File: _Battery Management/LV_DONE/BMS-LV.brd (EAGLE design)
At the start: 94.8 x 46.2 mm, 119 parts, among them J1 M1x5, J2 M1x4, J3 M1x4, J4 M1x4, J5 M1x2, J6 MX150L, J8 M1x5, J9 M80022232081-2, K1 ADJ14024, Q2 40V 0.2A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

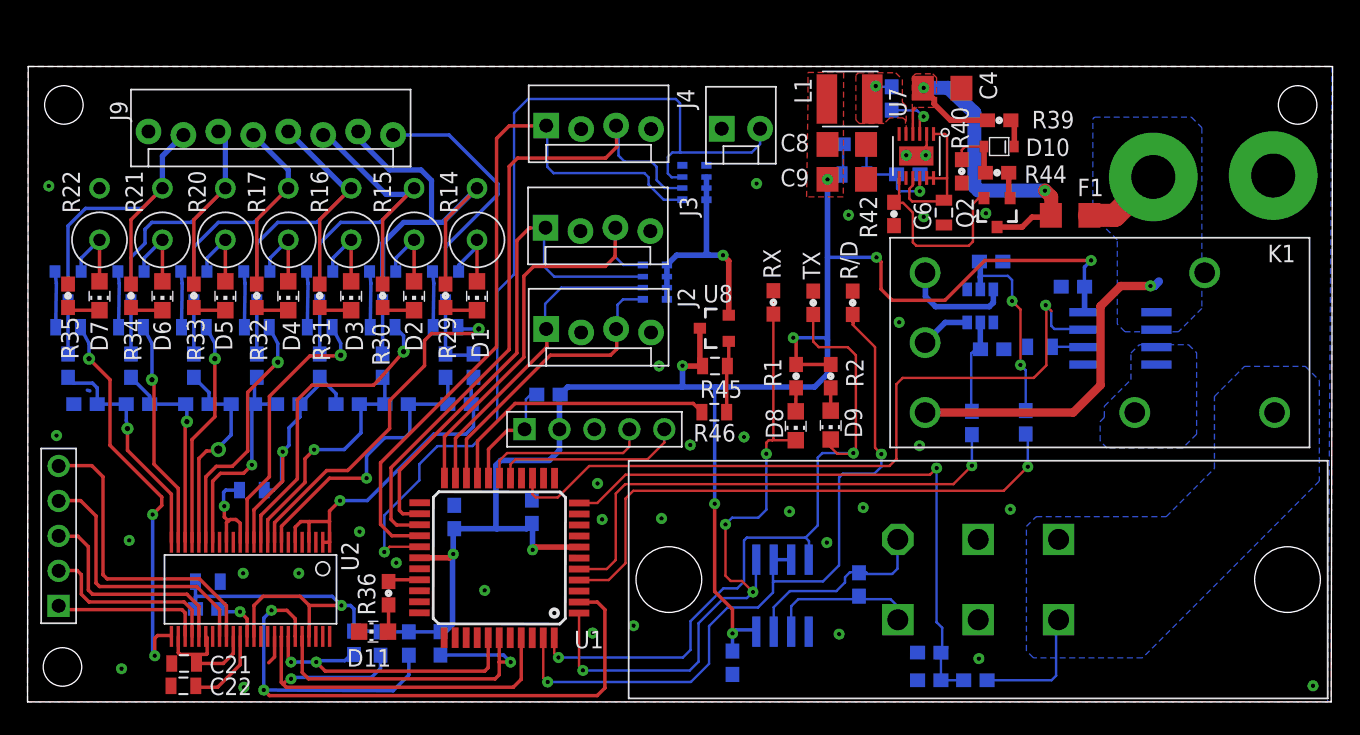
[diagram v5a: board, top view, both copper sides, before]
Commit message: 
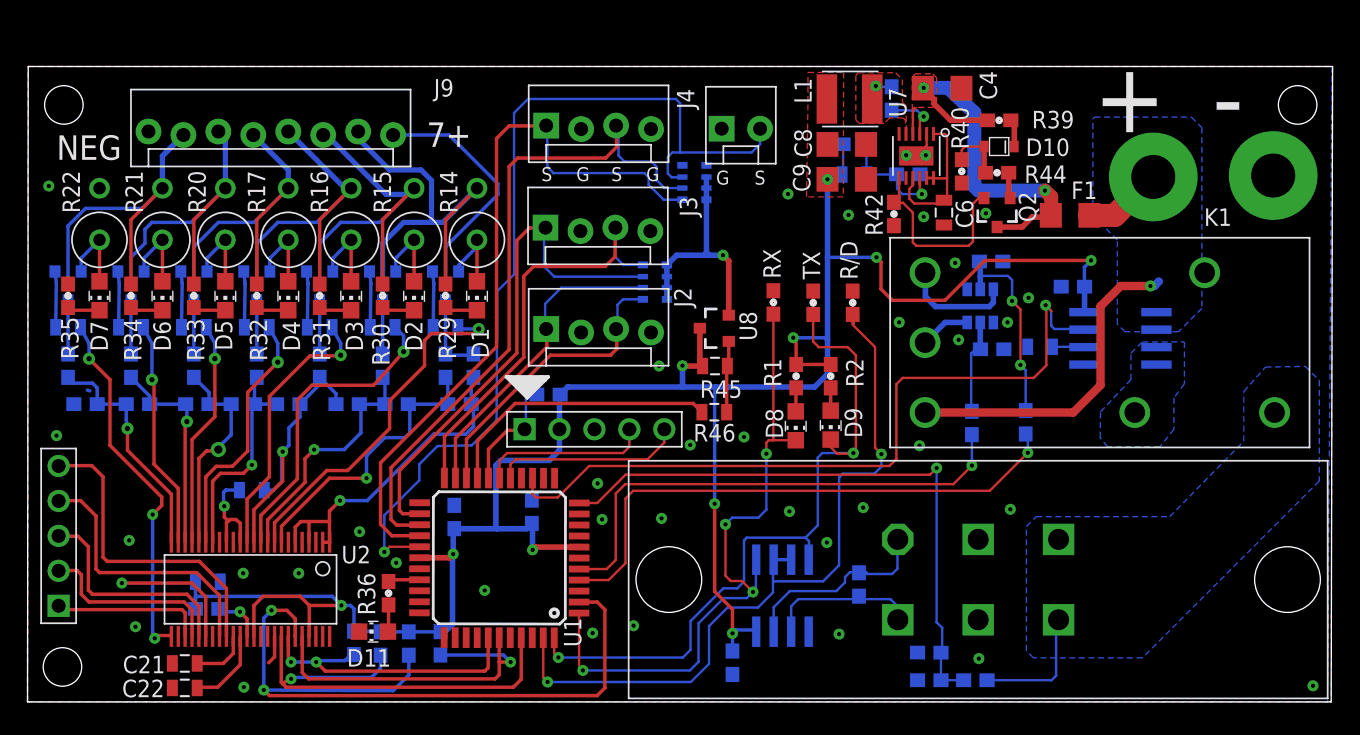
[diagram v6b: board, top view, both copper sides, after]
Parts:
- moved C22 0.18 mm to (11.4, 1.02)
- moved C21 0.05 mm to (11.4, 2.79)
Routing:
- net GND: track 9.08 -> 14.1 mm, vias 34 -> 39
- net S1: track 29.1 -> 26.6 mm
- net N$19: track 41.2 -> 40.6 mm
- net N$66: track 8.12 -> 8.63 mm
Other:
- board text added: "+"
- board text added: "-"
- board text added: "7+"
- board text added: "G"
- board text added: "NEG"
- board text added: "S"
